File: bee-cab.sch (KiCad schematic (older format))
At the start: 24 parts, among them J1 Conn_01x02_Male, J10 Conn_01x02, J11 Conn_01x01, J12 Conn_02x02_Odd_Even, J13 Conn_02x02_Odd_Even, J14 Conn_01x02, J15 Conn_01x02, J16 Conn_01x02, J17 Conn_01x02, J2 Conn_01x02_Male, J3 Conn_01x02_Male, J4 Conn_01x02_Male, J5 Conn_01x03, J6 Conn_02x04_Odd_Even, J7 Conn_02x04_Odd_Even, J8 Conn_02x01, J9 Conn_01x02

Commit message: Update schematic.
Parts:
- removed J7: Conn_02x04_Odd_Even, Connector_PinHeader_2.54mm:PinHeader_2x04_P2.54mm_Vertical, symbol Connector_Generic:Conn_02x04_Odd_Even
- removed R1: R_Variable, symbol Device:R_Variable
- added J7: Conn_01x02, Connector_PinHeader_2.54mm:PinHeader_2x01_P2.54mm_Vertical, symbol Connector_Generic:Conn_01x02
- added RV1: R_POT, Potentiometer_THT:Potentiometer_Bourns_3296W_Vertical, symbol Device:R_POT
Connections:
- net at C1.2: now also C2.2, J10.1 (Pin_1), J10.2 (Pin_2), J5.3 (Pin_3), J8.1 (Pin_1), R3.2, J7.1 (Pin_1)
- net at J13.1 (Pin_1), J13.3 (Pin_3), J15.1 (Pin_1)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: now also J7.2 (Pin_2)
- net at R2.1: now also RV1.2, RV1.3
- net at J8.2 (Pin_2): now also RV1.1
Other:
- moved on the sheet: J8, R2
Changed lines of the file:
@@
-	0    -1   1    0
-$EndComp
-$Comp
-L Connector_Generic:Conn_02x04_Odd_Even J7
-U 1 1 5CB4B56F
-P 3100 3250
-F 0 "J7" V 3104 2962 50  0000 R CNN
-F 1 "Conn_02x04_Odd_Even" V 3195 2962 50  0000 R CNN
-F 2 "Connector_PinHeader_2.54mm:PinHeader_2x04_P2.54mm_Vertical" H 3100 3250 50  0001 C CNN
-F 3 "~" H 3100 3250 50  0001 C CNN
-	1    3100 3250
 	0    -1   1    0
 $EndComp
@@
 	3200 1950 3300 1950
 Wire Wire Line
-	3000 2450 3000 2500
-Wire Wire Line
-	3000 2500 2600 2500
-Wire Wire Line
-	2600 2500 2600 2600
-Wire Wire Line
 	3100 2450 3100 2550
 Wire Wire Line
@@
 Wire Wire Line
 	3700 2450 3700 2550
-Wire Wire Line
-	2600 2900 2600 3000
-Wire Wire Line
-	3000 3000 3000 3050
-Wire Wire Line
-	3000 3000 2600 3000
-Wire Wire Line
-	3100 3050 3100 2950
-Wire Wire Line
-	3100 2950 3200 2950
-Wire Wire Line
-	3200 2950 3200 2900
-Wire Wire Line
-	3200 3050 3200 3000
-Wire Wire Line
-	3200 3000 3500 3000
-Wire Wire Line
-	3500 3000 3500 2900
 Wire Wire Line
 	3700 2550 3700 2650
@@
 Wire Wire Line
 	3700 2950 3700 3050
-Wire Wire Line
-	3700 3050 3300 3050
 Connection ~ 3700 2950
-Wire Wire Line
-	3000 3550 3100 3550
-Connection ~ 3100 3550
-Wire Wire Line
-	3100 3550 3150 3550
-Connection ~ 3200 3550
-Wire Wire Line
-	3200 3550 3300 3550
 $Comp
 L Device:R R4
@@
 L Device:R R2
 U 1 1 5CC02A28
-P 3400 4750
-F 0 "R2" H 3470 4796 50  0000 L CNN
-F 1 "R" H 3470 4705 50  0000 L CNN
-F 2 "Resistor_SMD:R_0805_2012Metric_Pad1.15x1.40mm_HandSolder" V 3330 4750 50  0001 C CNN
-F 3 "~" H 3400 4750 50  0001 C CNN
-	1    3400 4750
-	1    0    0    -1
-$EndComp
-$Comp
-L Device:R_Variable R1
-U 1 1 5CC03136
-P 3400 4350
-F 0 "R1" H 3528 4396 50  0000 L CNN
-F 1 "R_Variable" H 3528 4305 50  0000 L CNN
-F 2 "" V 3330 4350 50  0001 C CNN
-F 3 "~" H 3400 4350 50  0001 C CNN
-	1    3400 4350
-	1    0    0    -1
-$EndComp
-Wire Wire Line
-	3400 4600 3400 4500
+P 3500 4750
+F 0 "R2" H 3570 4796 50  0000 L CNN
+F 1 "R" H 3570 4705 50  0000 L CNN
+F 2 "Resistor_SMD:R_0805_2012Metric_Pad1.15x1.40mm_HandSolder" V 3430 4750 50  0001 C CNN
+F 3 "~" H 3500 4750 50  0001 C CNN
+	1    3500 4750
+	1    0    0    -1
+$EndComp
+Wire Wire Line
+	3500 4600 3500 4500
 $Comp
 L power:-15V #PWR06
@@
 Wire Wire Line
 	3150 4250 3150 3700
-Connection ~ 3150 3550
-Wire Wire Line
-	3150 3550 3200 3550
 Wire Wire Line
 	4200 5050 4500 5050
@@
 Wire Wire Line
 	5050 3050 5050 2900
+Connection ~ 3150 3700
+Connection ~ 3150 4950
+Wire Wire Line
+	3150 4950 3150 5050
+Wire Wire Line
+	5050 4350 5050 4200
+Wire Wire Line
+	5050 4200 5150 4200
+Wire Wire Line
+	5250 4200 5350 4200
+Wire Wire Line
+	5350 4800 5200 4800
+Wire Wire Line
+	5050 4800 5050 4650
+Wire Wire Line
+	5200 4800 5200 5050
+Wire Wire Line
+	4500 5050 5200 5050
+Connection ~ 5200 4800
+Wire Wire Line
+	5200 4800 5050 4800
+Wire Wire Line
+	5150 3700 5200 3700
+Wire Wire Line
+	5200 3700 5200 3400
+Connection ~ 5200 3700
+Wire Wire Line
+	5200 3700 5250 3700
+Connection ~ 5200 3050
+Wire Wire Line
+	5200 3050 5050 3050
+Wire Wire Line
+	3150 3050 3150 3300
+Connection ~ 3150 3050
+Wire Wire Line
+	3000 2550 2600 2550
+Wire Wire Line
+	2600 2550 2600 2600
+Wire Wire Line
+	3000 2450 3000 2550
+Wire Wire Line
+	2600 2900 2600 3050
+Wire Wire Line
+	2600 3050 3150 3050
+Wire Wire Line
+	3150 3050 3200 3050
+Wire Wire Line
+	3200 2900 3200 3050
+Connection ~ 3200 3050
+Wire Wire Line
+	3200 3050 3500 3050
+Wire Wire Line
+	3500 2900 3500 3050
+Connection ~ 3500 3050
+Wire Wire Line
+	3500 3050 3700 3050
+$Comp
+L Connector_Generic:Conn_01x02 J7
+U 1 1 5CC2FF5F
+P 5700 3300
+F 0 "J7" H 5780 3292 50  0000 L CNN
+F 1 "Conn_01x02" H 5780 3201 50  0000 L CNN
+F 2 "Connector_PinHeader_2.54mm:PinHeader_2x01_P2.54mm_Vertical" H 5700 3300 50  0001 C CNN
+F 3 "~" H 5700 3300 50  0001 C CNN
+	1    5700 3300
+	1    0    0    -1
+$EndComp
+Wire Wire Line
+	5500 3300 3150 3300
+Connection ~ 3150 3300
+Wire Wire Line
+	3150 3300 3150 3700
+Wire Wire Line
+	5500 3400 5200 3400
+Connection ~ 5200 3400
+Wire Wire Line
+	5200 3400 5200 3050
+$Comp
+L Device:R_POT RV1
+U 1 1 5CC3714E
+P 3500 4350
+F 0 "RV1" H 3431 4396 50  0000 R CNN
+F 1 "R_POT" H 3431 4305 50  0000 R CNN
+F 2 "Potentiometer_THT:Potentiometer_Bourns_3296W_Vertical" H 3500 4350 50  0001 C CNN
+F 3 "~" H 3500 4350 50  0001 C CNN
+	1    3500 4350
+	1    0    0    -1
+$EndComp
 $Comp
 L Connector_Generic:Conn_02x01 J8
 U 1 1 5CC269B0
-P 3400 3900
-F 0 "J8" V 3404 3980 50  0000 L CNN
-F 1 "Conn_02x01" V 3495 3980 50  0000 L CNN
-F 2 "Connector_PinHeader_2.54mm:PinHeader_2x01_P2.54mm_Vertical" H 3400 3900 50  0001 C CNN
-F 3 "~" H 3400 3900 50  0001 C CNN
-	1    3400 3900
+P 3500 3900
+F 0 "J8" V 3504 3980 50  0000 L CNN
+F 1 "Conn_02x01" V 3595 3980 50  0000 L CNN
+F 2 "Connector_PinHeader_2.54mm:PinHeader_2x01_P2.54mm_Vertical" H 3500 3900 50  0001 C CNN
+F 3 "~" H 3500 3900 50  0001 C CNN
+	1    3500 3900
 	0    1    1    0
 $EndComp
 Wire Wire Line
-	3400 3700 3150 3700
-Connection ~ 3150 3700
-Wire Wire Line
-	3150 3700 3150 3550
-Wire Wire Line
-	3400 4900 3400 4950
-Wire Wire Line
-	3400 4950 3150 4950
-Connection ~ 3150 4950
-Wire Wire Line
-	3150 4950 3150 5050
-Wire Wire Line
-	5050 4350 5050 4200
-Wire Wire Line
-	5050 4200 5150 4200
-Wire Wire Line
-	5250 4200 5350 4200
-Wire Wire Line
-	5350 4800 5200 4800
-Wire Wire Line
-	5050 4800 5050 4650
-Wire Wire Line
-	5200 4800 5200 5050
-Wire Wire Line
-	4500 5050 5200 5050
-Connection ~ 5200 4800
-Wire Wire Line
-	5200 4800 5050 4800
-Wire Wire Line
-	5150 3700 5200 3700
-Wire Wire Line
-	5200 3700 5200 3050
-Connection ~ 5200 3700
-Wire Wire Line
-	5200 3700 5250 3700
-Connection ~ 5200 3050
-Wire Wire Line
-	5200 3050 5050 3050
+	3150 3700 3500 3700
+Wire Wire Line
+	3500 4950 3500 4900
+Wire Wire Line
+	3150 4950 3500 4950
+Wire Wire Line
+	3650 4350 3650 4500
+Wire Wire Line
+	3650 4500 3500 4500
+Connection ~ 3500 4500
 $EndSCHEMATC

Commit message: Update schematic.
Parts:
- removed J7: Conn_01x02, Connector_PinHeader_2.54mm:PinHeader_2x01_P2.54mm_Vertical, symbol Connector_Generic:Conn_01x02
- added J17: Conn_01x03, Connector_PinHeader_2.54mm:PinHeader_1x03_P2.54mm_Vertical, symbol Connector_Generic:Conn_01x03
- C1: footprint (none) -> Capacitor_THT-emt:C_Trimmer_Vishay_D10mm_Vertical_HolePattern5mmx10mm
- renumbered J11 to J10, J12 to J11, J13 to J12, J14 to J13, J15 to J14, J16 to J15, J17 to J16, J8 to J7, J9 to J8, J10 to J9, R3 to R1, R4 to R3, R5 to R4
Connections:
- net GND: now also J17.2 (Pin_2)
- net at C1.2, C2.2, J5.3 (Pin_3)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: now also J17.1 (Pin_1)
- net at J12.1 (Pin_1), J12.3 (Pin_3), J14.1 (Pin_1)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: now also J17.3 (Pin_3)
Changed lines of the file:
@@
 F 0 "C1" H 2715 2796 50  0000 L CNN
 F 1 "C_Variable" H 2715 2705 50  0000 L CNN
-F 2 "" H 2600 2750 50  0001 C CNN
+F 2 "Capacitor_THT-emt:C_Trimmer_Vishay_D10mm_Vertical_HolePattern5mmx10mm" H 2600 2750 50  0001 C CNN
 F 3 "~" H 2600 2750 50  0001 C CNN
 	1    2600 2750
@@
 $EndComp
 $Comp
-L Connector_Generic:Conn_01x02 J9
+L Connector_Generic:Conn_01x02 J8
 U 1 1 5CB4A9D0
 P 3900 2550
-F 0 "J9" H 3980 2542 50  0000 L CNN
+F 0 "J8" H 3980 2542 50  0000 L CNN
 F 1 "Conn_01x02" H 3980 2451 50  0000 L CNN
 F 2 "Connector_PinSocket_2.54mm:PinSocket_2x01_P2.54mm_Vertical" H 3900 2550 50  0001 C CNN
@@
 $EndComp
 $Comp
-L Connector_Generic:Conn_01x02 J10
+L Connector_Generic:Conn_01x02 J9
 U 1 1 5CB4AA40
 P 3900 2850
-F 0 "J10" H 3980 2842 50  0000 L CNN
+F 0 "J9" H 3980 2842 50  0000 L CNN
 F 1 "Conn_01x02" H 3980 2751 50  0000 L CNN
 F 2 "Connector_PinSocket_2.54mm:PinSocket_2x01_P2.54mm_Vertical" H 3900 2850 50  0001 C CNN
@@
 $EndComp
 $Comp
-L Device:R R3
+L Device:R R1
 U 1 1 5CB4AE05
 P 3500 2750
-F 0 "R3" H 3570 2796 50  0000 L CNN
+F 0 "R1" H 3570 2796 50  0000 L CNN
 F 1 "R" H 3570 2705 50  0000 L CNN
 F 2 "Resistor_SMD:R_0805_2012Metric_Pad1.15x1.40mm_HandSolder" V 3430 2750 50  0001 C CNN
@@
 Connection ~ 3700 2950
 $Comp
-L Device:R R4
+L Device:R R3
 U 1 1 5CB50577
 P 5050 2750
-F 0 "R4" H 5120 2796 50  0000 L CNN
+F 0 "R3" H 5120 2796 50  0000 L CNN
 F 1 "R" H 5120 2705 50  0000 L CNN
 F 2 "Resistor_SMD:R_0805_2012Metric_Pad1.15x1.40mm_HandSolder" V 4980 2750 50  0001 C CNN
@@
 $EndComp
 $Comp
-L Device:R R5
+L Device:R R4
 U 1 1 5CB50759
 P 5050 4500
-F 0 "R5" H 5120 4546 50  0000 L CNN
+F 0 "R4" H 5120 4546 50  0000 L CNN
 F 1 "R" H 5120 4455 50  0000 L CNN
 F 2 "Resistor_SMD:R_0805_2012Metric_Pad1.15x1.40mm_HandSolder" V 4980 4500 50  0001 C CNN
@@
 Connection ~ 4150 1800
 $Comp
-L Connector_Generic:Conn_01x01 J11
+L Connector_Generic:Conn_01x01 J10
 U 1 1 5CC0CCD3
 P 4500 4850
-F 0 "J11" V 4464 4762 50  0000 R CNN
+F 0 "J10" V 4464 4762 50  0000 R CNN
 F 1 "Conn_01x01" V 4373 4762 50  0000 R CNN
 F 2 "Connector_PinHeader_2.54mm:PinHeader_1x01_P2.54mm_Vertical" H 4500 4850 50  0001 C CNN
@@
 Connection ~ 4500 5050
 $Comp
-L Connector_Generic:Conn_01x02 J16
+L Connector_Generic:Conn_01x02 J15
 U 1 1 5CC09F7D
 P 5550 4300
-F 0 "J16" H 5630 4292 50  0000 L CNN
+F 0 "J15" H 5630 4292 50  0000 L CNN
 F 1 "Conn_01x02" H 5630 4201 50  0000 L CNN
 F 2 "Connector_PinSocket_2.54mm:PinSocket_2x01_P2.54mm_Vertical" H 5550 4300 50  0001 C CNN
@@
 $EndComp
 $Comp
-L Connector_Generic:Conn_01x02 J17
+L Connector_Generic:Conn_01x02 J16
 U 1 1 5CC09F87
 P 5550 4600
-F 0 "J17" H 5630 4592 50  0000 L CNN
+F 0 "J16" H 5630 4592 50  0000 L CNN
 F 1 "Conn_01x02" H 5630 4501 50  0000 L CNN
 F 2 "Connector_PinSocket_2.54mm:PinSocket_2x01_P2.54mm_Vertical" H 5550 4600 50  0001 C CNN
@@
 Connection ~ 5350 4700
 $Comp
-L Connector_Generic:Conn_01x02 J14
+L Connector_Generic:Conn_01x02 J13
 U 1 1 5CC12845
 P 5550 2550
-F 0 "J14" H 5630 2542 50  0000 L CNN
+F 0 "J13" H 5630 2542 50  0000 L CNN
 F 1 "Conn_01x02" H 5630 2451 50  0000 L CNN
 F 2 "Connector_PinSocket_2.54mm:PinSocket_2x01_P2.54mm_Vertical" H 5550 2550 50  0001 C CNN
@@
 $EndComp
 $Comp
-L Connector_Generic:Conn_01x02 J15
+L Connector_Generic:Conn_01x02 J14
 U 1 1 5CC1284F
 P 5550 2850
-F 0 "J15" H 5630 2842 50  0000 L CNN
+F 0 "J14" H 5630 2842 50  0000 L CNN
 F 1 "Conn_01x02" H 5630 2751 50  0000 L CNN
 F 2 "Connector_PinSocket_2.54mm:PinSocket_2x01_P2.54mm_Vertical" H 5550 2850 50  0001 C CNN
@@
 Connection ~ 5350 2950
 $Comp
-L Connector_Generic:Conn_02x02_Odd_Even J12
+L Connector_Generic:Conn_02x02_Odd_Even J11
 U 1 1 5CC15D49
 P 5150 2150
-F 0 "J12" V 5154 1962 50  0000 R CNN
+F 0 "J11" V 5154 1962 50  0000 R CNN
 F 1 "Conn_02x02_Odd_Even" V 5245 1962 50  0000 R CNN
 F 2 "Connector_PinHeader_2.54mm:PinHeader_2x02_P2.54mm_Vertical" H 5150 2150 50  0001 C CNN
@@
 $EndComp
 $Comp
-L Connector_Generic:Conn_02x02_Odd_Even J13
+L Connector_Generic:Conn_02x02_Odd_Even J12
 U 1 1 5CC1719B
 P 5150 3900
-F 0 "J13" V 5154 3712 50  0000 R CNN
+F 0 "J12" V 5154 3712 50  0000 R CNN
 F 1 "Conn_02x02_Odd_Even" V 5245 3712 50  0000 R CNN
 F 2 "Connector_PinHeader_2.54mm:PinHeader_2x02_P2.54mm_Vertical" H 5150 3900 50  0001 C CNN
@@
 	5150 3700 5200 3700
 Wire Wire Line
-	5200 3700 5200 3400
+	5200 3700 5200 3500
 Connection ~ 5200 3700
 Wire Wire Line
@@
 Wire Wire Line
 	3500 3050 3700 3050
-$Comp
-L Connector_Generic:Conn_01x02 J7
-U 1 1 5CC2FF5F
-P 5700 3300
-F 0 "J7" H 5780 3292 50  0000 L CNN
-F 1 "Conn_01x02" H 5780 3201 50  0000 L CNN
-F 2 "Connector_PinHeader_2.54mm:PinHeader_2x01_P2.54mm_Vertical" H 5700 3300 50  0001 C CNN
-F 3 "~" H 5700 3300 50  0001 C CNN
-	1    5700 3300
-	1    0    0    -1
-$EndComp
 Wire Wire Line
 	5500 3300 3150 3300
@@
 	3150 3300 3150 3700
 Wire Wire Line
-	5500 3400 5200 3400
-Connection ~ 5200 3400
-Wire Wire Line
-	5200 3400 5200 3050
+	5500 3500 5200 3500
 $Comp
 L Device:R_POT RV1
@@
 $EndComp
 $Comp
-L Connector_Generic:Conn_02x01 J8
+L Connector_Generic:Conn_02x01 J7
 U 1 1 5CC269B0
 P 3500 3900
-F 0 "J8" V 3504 3980 50  0000 L CNN
+F 0 "J7" V 3504 3980 50  0000 L CNN
 F 1 "Conn_02x01" V 3595 3980 50  0000 L CNN
 F 2 "Connector_PinHeader_2.54mm:PinHeader_2x01_P2.54mm_Vertical" H 3500 3900 50  0001 C CNN
@@
 	3650 4500 3500 4500
 Connection ~ 3500 4500
+$Comp
+L Connector_Generic:Conn_01x03 J17
+U 1 1 5CC3261E
+P 5700 3400
+F 0 "J17" H 5780 3442 50  0000 L CNN
+F 1 "Conn_01x03" H 5780 3351 50  0000 L CNN
+F 2 "Connector_PinHeader_2.54mm:PinHeader_1x03_P2.54mm_Vertical" H 5700 3400 50  0001 C CNN
+F 3 "~" H 5700 3400 50  0001 C CNN
+	1    5700 3400
+	1    0    0    -1
+$EndComp
+Connection ~ 5200 3500
+Wire Wire Line
+	5200 3050 5200 3500
+$Comp
+L power:GND #PWR07
+U 1 1 5CC3509D
+P 5400 3400
+F 0 "#PWR07" H 5400 3150 50  0001 C CNN
+F 1 "GND" H 5405 3227 50  0000 C CNN
+F 2 "" H 5400 3400 50  0001 C CNN
+F 3 "" H 5400 3400 50  0001 C CNN
+	1    5400 3400
+	1    0    0    -1
+$EndComp
+Wire Wire Line
+	5400 3400 5500 3400
 $EndSCHEMATC

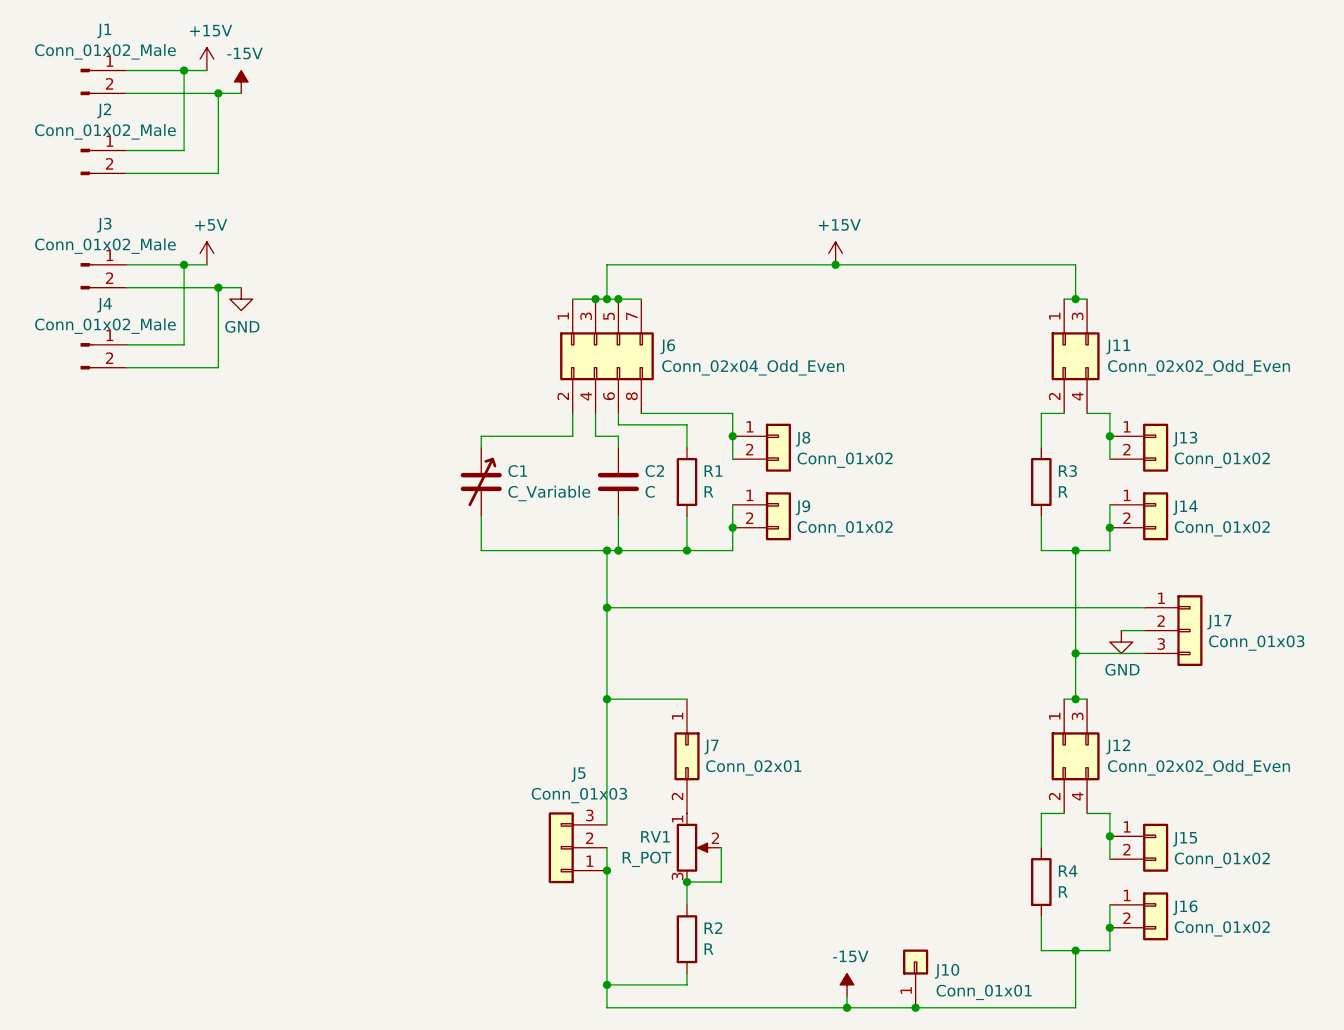
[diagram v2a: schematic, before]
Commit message: Remove unnecessary jumpers.
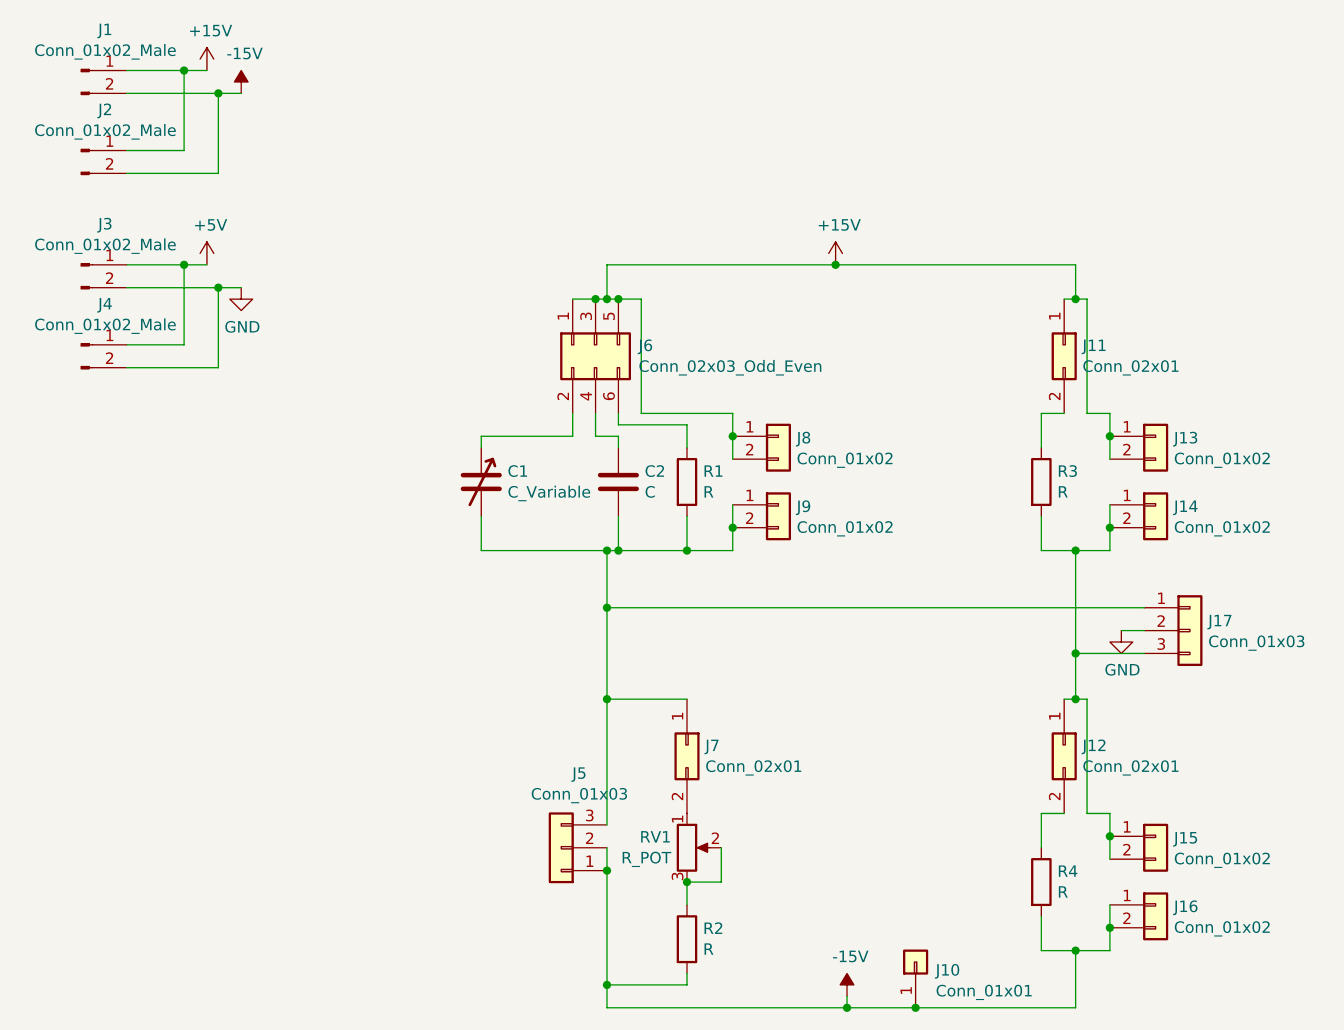
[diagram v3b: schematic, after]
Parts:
- removed J11, J12: Conn_02x02_Odd_Even, Connector_PinHeader_2.54mm:PinHeader_2x02_P2.54mm_Vertical, symbol Connector_Generic:Conn_02x02_Odd_Even
- removed J6: Conn_02x04_Odd_Even, Connector_PinHeader_2.54mm:PinHeader_2x04_P2.54mm_Vertical, symbol Connector_Generic:Conn_02x04_Odd_Even
- added J11, J12: Conn_02x01, Connector_PinHeader_2.54mm:PinHeader_2x01_P2.54mm_Vertical, symbol Connector_Generic:Conn_02x01
- added J6: Conn_02x03_Odd_Even, Connector_PinHeader_2.54mm:PinHeader_2x03_P2.54mm_Vertical, symbol Connector_Generic:Conn_02x03_Odd_Even
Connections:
- net +15V: now also J13.1 (Pin_1), J13.2 (Pin_2), J8.1 (Pin_1), J8.2 (Pin_2), J11.1 (Pin_1), J6.1 (Pin_1), J6.3 (Pin_3), J6.5 (Pin_5)
- net at C1.1: now also J6.2 (Pin_2)
- net at C2.1: now also J6.4 (Pin_4)
- net at R1.1: now also J6.6 (Pin_6)
- net at R3.1: now also J11.2 (Pin_2)
- net at J14.1 (Pin_1), J14.2 (Pin_2), J17.3 (Pin_3)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: now also J15.1 (Pin_1), J15.2 (Pin_2), J12.1 (Pin_1)
- net at R4.1: now also J12.2 (Pin_2)
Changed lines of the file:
@@
 	1    0    0    -1
 $EndComp
-$Comp
-L Connector_Generic:Conn_02x04_Odd_Even J6
-U 1 1 5CB4B44B
-P 3100 2150
-F 0 "J6" V 3104 1862 50  0000 R CNN
-F 1 "Conn_02x04_Odd_Even" V 3195 1862 50  0000 R CNN
-F 2 "Connector_PinHeader_2.54mm:PinHeader_2x04_P2.54mm_Vertical" H 3100 2150 50  0001 C CNN
-F 3 "~" H 3100 2150 50  0001 C CNN
-	1    3100 2150
-	0    -1   1    0
-$EndComp
-Wire Wire Line
-	3000 1950 3100 1950
-Connection ~ 3100 1950
-Wire Wire Line
-	3100 1950 3150 1950
-Connection ~ 3200 1950
-Wire Wire Line
-	3200 1950 3300 1950
 Wire Wire Line
 	3100 2450 3100 2550
@@
 	3150 1800 3150 1950
 Connection ~ 3150 1950
-Wire Wire Line
-	3150 1950 3200 1950
 Wire Wire Line
 	3150 4350 3150 4450
@@
 	5350 2950 5350 3050
 Connection ~ 5350 2950
-$Comp
-L Connector_Generic:Conn_02x02_Odd_Even J11
-U 1 1 5CC15D49
-P 5150 2150
-F 0 "J11" V 5154 1962 50  0000 R CNN
-F 1 "Conn_02x02_Odd_Even" V 5245 1962 50  0000 R CNN
-F 2 "Connector_PinHeader_2.54mm:PinHeader_2x02_P2.54mm_Vertical" H 5150 2150 50  0001 C CNN
-F 3 "~" H 5150 2150 50  0001 C CNN
-	1    5150 2150
-	0    -1   1    0
-$EndComp
-$Comp
-L Connector_Generic:Conn_02x02_Odd_Even J12
-U 1 1 5CC1719B
-P 5150 3900
-F 0 "J12" V 5154 3712 50  0000 R CNN
-F 1 "Conn_02x02_Odd_Even" V 5245 3712 50  0000 R CNN
-F 2 "Connector_PinHeader_2.54mm:PinHeader_2x02_P2.54mm_Vertical" H 5150 3900 50  0001 C CNN
-F 3 "~" H 5150 3900 50  0001 C CNN
-	1    5150 3900
-	0    -1   1    0
-$EndComp
 Wire Wire Line
 	5200 1800 5200 1950
@@
 Wire Wire Line
 	5400 3400 5500 3400
+Wire Wire Line
+	3150 1950 3200 1950
+$Comp
+L Connector_Generic:Conn_02x03_Odd_Even J6
+U 1 1 5CC3C4A8
+P 3100 2150
+F 0 "J6" V 3104 1962 50  0000 R CNN
+F 1 "Conn_02x03_Odd_Even" V 3195 1962 50  0000 R CNN
+F 2 "Connector_PinHeader_2.54mm:PinHeader_2x03_P2.54mm_Vertical" H 3100 2150 50  0001 C CNN
+F 3 "~" H 3100 2150 50  0001 C CNN
+	1    3100 2150
+	0    -1   1    0
+$EndComp
+Wire Wire Line
+	3100 1950 3150 1950
+Connection ~ 3200 1950
+Wire Wire Line
+	3200 1950 3300 1950
+Wire Wire Line
+	3000 1950 3100 1950
+Connection ~ 3100 1950
+Wire Wire Line
+	3300 2450 3300 1950
+$Comp
+L Connector_Generic:Conn_02x01 J11
+U 1 1 5CC423CE
+P 5150 2150
+F 0 "J11" V 5154 2230 50  0000 L CNN
+F 1 "Conn_02x01" V 5245 2230 50  0000 L CNN
+F 2 "Connector_PinHeader_2.54mm:PinHeader_2x01_P2.54mm_Vertical" H 5150 2150 50  0001 C CNN
+F 3 "~" H 5150 2150 50  0001 C CNN
+	1    5150 2150
+	0    1    1    0
+$EndComp
+Wire Wire Line
+	5250 2450 5250 1950
+$Comp
+L Connector_Generic:Conn_02x01 J12
+U 1 1 5CC45458
+P 5150 3900
+F 0 "J12" V 5154 3980 50  0000 L CNN
+F 1 "Conn_02x01" V 5245 3980 50  0000 L CNN
+F 2 "Connector_PinHeader_2.54mm:PinHeader_2x01_P2.54mm_Vertical" H 5150 3900 50  0001 C CNN
+F 3 "~" H 5150 3900 50  0001 C CNN
+	1    5150 3900
+	0    1    1    0
+$EndComp
+Wire Wire Line
+	5250 4200 5250 3700
 $EndSCHEMATC
